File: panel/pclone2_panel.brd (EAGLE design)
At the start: 86 x 88.5 mm, 17 parts

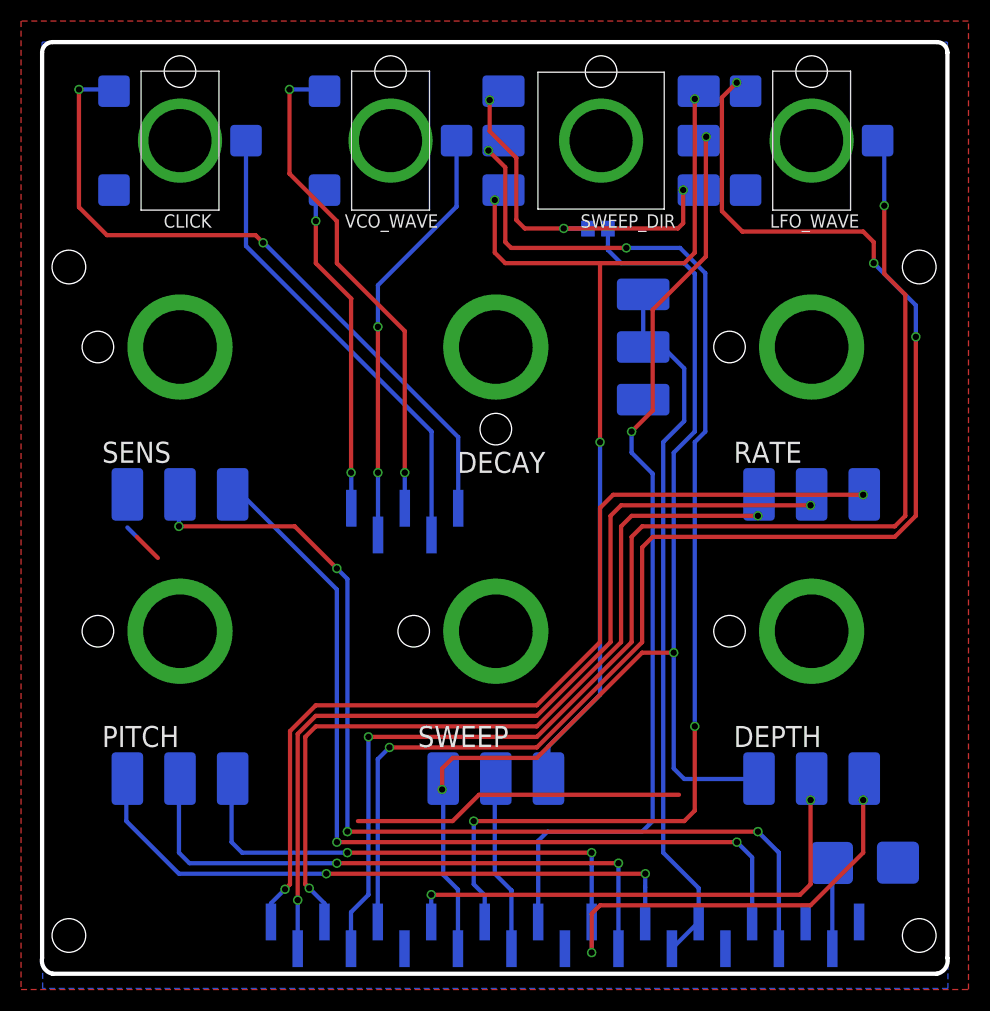
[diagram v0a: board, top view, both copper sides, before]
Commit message: V4 Panel
Moved tracks away from hole. Added extra hole for piezo wires. Additional ground plane clearance
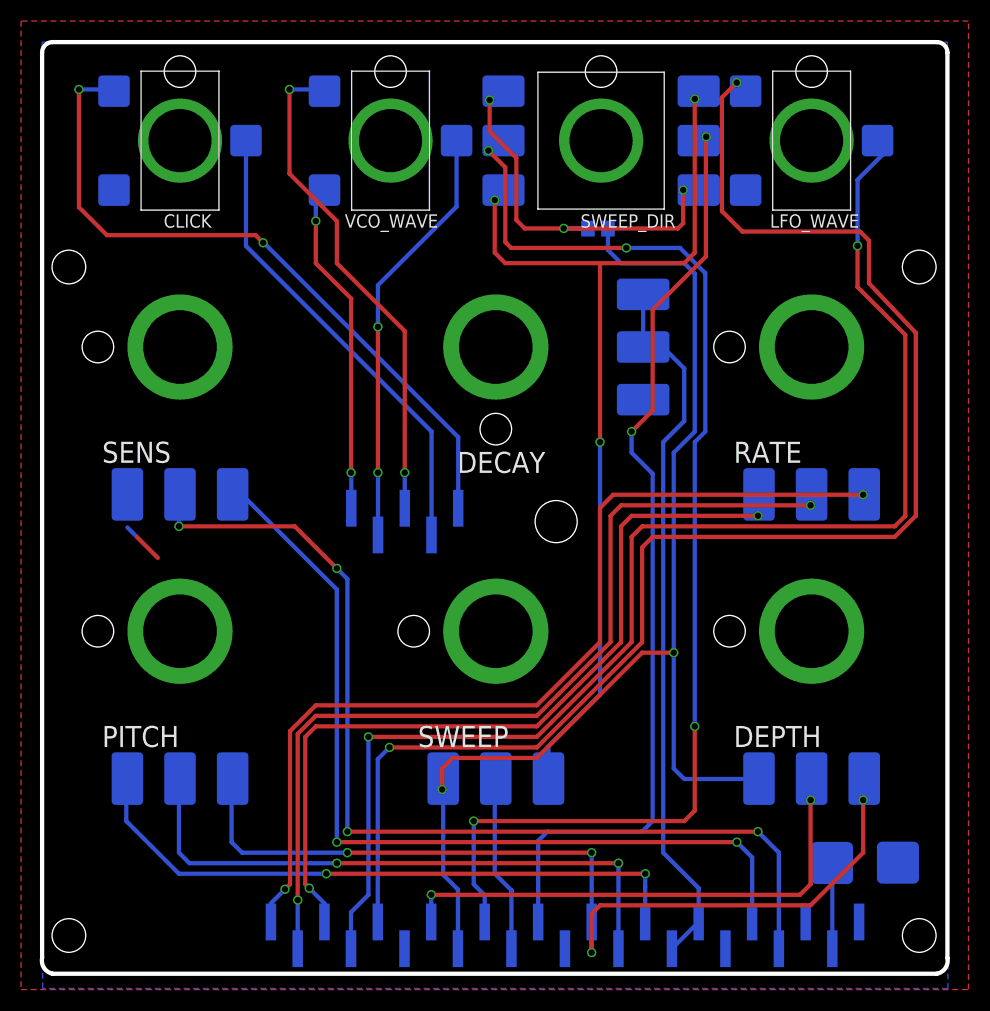
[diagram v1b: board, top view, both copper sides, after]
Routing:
- net GND: track 35.6 -> 4.10 mm
- net MODSHAPE2: track 124.5 -> 126.1 mm
- net MODSHAPE1: track 139.3 -> 139.0 mm, vias 4 -> 2
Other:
- board text added: "PCLONE2 CONTROL PANEL PCB V4"
- board text removed: "PCLONE2 CONTROL PANEL PCB V3"
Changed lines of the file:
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@@
 <text x="33.274" y="54.483" size="1.778" layer="22" font="vector" rot="MR0">SENS
 A100K</text>
-<text x="55.462" y="47.603" size="1.778" layer="22" font="vector" rot="MR0">DECAY
+<text x="49.874" y="47.857" size="1.778" layer="22" font="vector" rot="MR0">DECAY
 A1M</text>
 <text x="60.23" y="56.118" size="1.778" layer="22" font="vector" rot="MR180">RATE
@@
 <text x="86.995" y="73.406" size="1.778" layer="22" font="vector" rot="MR0">LFO WAVE</text>
 <text x="77.28" y="18.583" size="1.778" layer="22" font="vector" rot="MR180">-TRIG+</text>
-<text x="6.521" y="58.042" size="1.6" layer="22" font="vector" rot="MR270">PCLONE2 CONTROL PANEL PCB V3</text>
+<text x="6.521" y="58.042" size="1.6" layer="22" font="vector" rot="MR270">PCLONE2 CONTROL PANEL PCB V4</text>
 <text x="87.439" y="26.285" size="1.6" layer="22" font="vector" rot="MR90">SIXTY FOUR PIXELS LTD</text>
 <rectangle x1="12.105159375" y1="6.4262" x2="19.725159375" y2="6.45668125" layer="52"/>
@@
 <wire x1="44.85" y1="48.55" x2="31.95" y2="48.55" width="0.4064" layer="22"/>
 <wire x1="43.35" y1="44.55" x2="31.95" y2="44.55" width="0.4064" layer="22"/>
+<hole x="52.832" y="46.45" drill="4"/>
 </plain>
 <attributes>
@@
 <contactref element="SWEEP_DIR" pad="BODY"/>
 <contactref element="LFO_WAVE" pad="BODY"/>
-<polygon width="0.4064" layer="16">
+<polygon width="0.4064" layer="16" isolate="0.8128">
 <vertex x="4" y="92"/>
 <vertex x="90" y="92"/>
@@
 <wire x1="12.1" y1="45.9" x2="13" y2="45" width="0.4064" layer="16"/>
 <wire x1="13" y1="45" x2="15" y2="43" width="0.4064" layer="1"/>
-<wire x1="64.5" y1="20.5" x2="45.5" y2="20.5" width="0.4064" layer="1"/>
-<wire x1="45.5" y1="20.5" x2="43" y2="18" width="0.4064" layer="1"/>
-<wire x1="43" y1="18" x2="34" y2="18" width="0.4064" layer="1"/>
 <contactref element="JP3" pad="1"/>
 <contactref element="JP3" pad="3"/>
@@
 <wire x1="62" y1="45" x2="85" y2="45" width="0.4064" layer="1"/>
 <wire x1="85" y1="45" x2="87" y2="47" width="0.4064" layer="1"/>
-<wire x1="87" y1="47" x2="87" y2="64" width="0.4064" layer="1"/>
-<via x="87" y="64" extent="1-16" drill="0.6"/>
+<wire x1="87" y1="47" x2="87" y2="64.384" width="0.4064" layer="1"/>
 <contactref element="LFO_WAVE" pad="B"/>
 <via x="69.984" y="88.15" extent="1-16" drill="0.6"/>
 <wire x1="71" y1="87.171" x2="70.83" y2="87.341" width="0.4064" layer="16"/>
-<wire x1="70.526" y1="74" x2="82" y2="74" width="0.4064" layer="1"/>
-<wire x1="82" y1="74" x2="83" y2="73" width="0.4064" layer="1"/>
-<wire x1="83" y1="73" x2="83" y2="71" width="0.4064" layer="1"/>
-<via x="83" y="71" extent="1-16" drill="0.6"/>
-<wire x1="83" y1="71" x2="87" y2="67" width="0.4064" layer="16"/>
-<wire x1="87" y1="67" x2="87" y2="64" width="0.4064" layer="16"/>
+<wire x1="70.526" y1="74" x2="81.702" y2="74" width="0.4064" layer="1"/>
 <contactref element="JP4" pad="9"/>
 <wire x1="35.885" y1="8.42" x2="35.885" y2="23.885" width="0.4064" layer="16"/>
@@
 <wire x1="68.58" y1="75.946" x2="68.58" y2="86.746" width="0.4064" layer="1"/>
 <wire x1="68.58" y1="86.746" x2="69.984" y2="88.15" width="0.4064" layer="1"/>
+<wire x1="87" y1="64.384" x2="82.55" y2="69.088" width="0.4064" layer="1"/>
+<wire x1="81.702" y1="74" x2="82.55" y2="73.152" width="0.4064" layer="1"/>
+<wire x1="82.55" y1="69.088" x2="82.55" y2="73.152" width="0.4064" layer="1"/>
 </signal>
 <signal name="MODSHAPE2">
@@
 <wire x1="61" y1="46" x2="85" y2="46" width="0.4064" layer="1"/>
 <wire x1="85" y1="46" x2="86" y2="47" width="0.4064" layer="1"/>
-<wire x1="86" y1="47" x2="86" y2="68" width="0.4064" layer="1"/>
+<wire x1="86" y1="47" x2="86" y2="64.19" width="0.4064" layer="1"/>
 <wire x1="83" y1="82.271" x2="83.37" y2="82.641" width="0.4064" layer="16"/>
-<wire x1="86" y1="68" x2="84" y2="70" width="0.4064" layer="1"/>
-<wire x1="84" y1="70" x2="84" y2="76.46" width="0.4064" layer="1"/>
-<via x="84" y="76.46" extent="1-16" drill="0.6"/>
-<wire x1="84" y1="76.46" x2="84" y2="83" width="0.4064" layer="16"/>
+<wire x1="81.46" y1="68.73" x2="81.46" y2="72.65" width="0.4064" layer="1"/>
+<via x="81.46" y="72.65" extent="1-16" drill="0.6"/>
 <wire x1="84" y1="83" x2="83.729" y2="83" width="0.4064" layer="16"/>
 <wire x1="83.729" y1="83" x2="83.37" y2="82.641" width="0.4064" layer="16"/>
 <contactref element="JP4" pad="10"/>
 <wire x1="33.345" y1="5.88" x2="33.345" y2="9.345" width="0.4064" layer="16"/>
+<wire x1="81.46" y1="68.73" x2="86" y2="64.19" width="0.4064" layer="1"/>
+<wire x1="81.46" y1="72.65" x2="81.46" y2="78.92" width="0.4064" layer="16"/>
+<wire x1="81.46" y1="78.92" x2="83.82" y2="81.28" width="0.4064" layer="16"/>
+<wire x1="83.82" y1="81.28" x2="83.82" y2="81.451" width="0.4064" layer="16"/>
+<wire x1="83.82" y1="81.451" x2="83" y2="82.271" width="0.4064" layer="16"/>
 </signal>
 <signal name="MODRATE1">
